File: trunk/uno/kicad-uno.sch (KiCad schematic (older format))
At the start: 16 parts, among them J1 RESET_EN, SW1 RESET

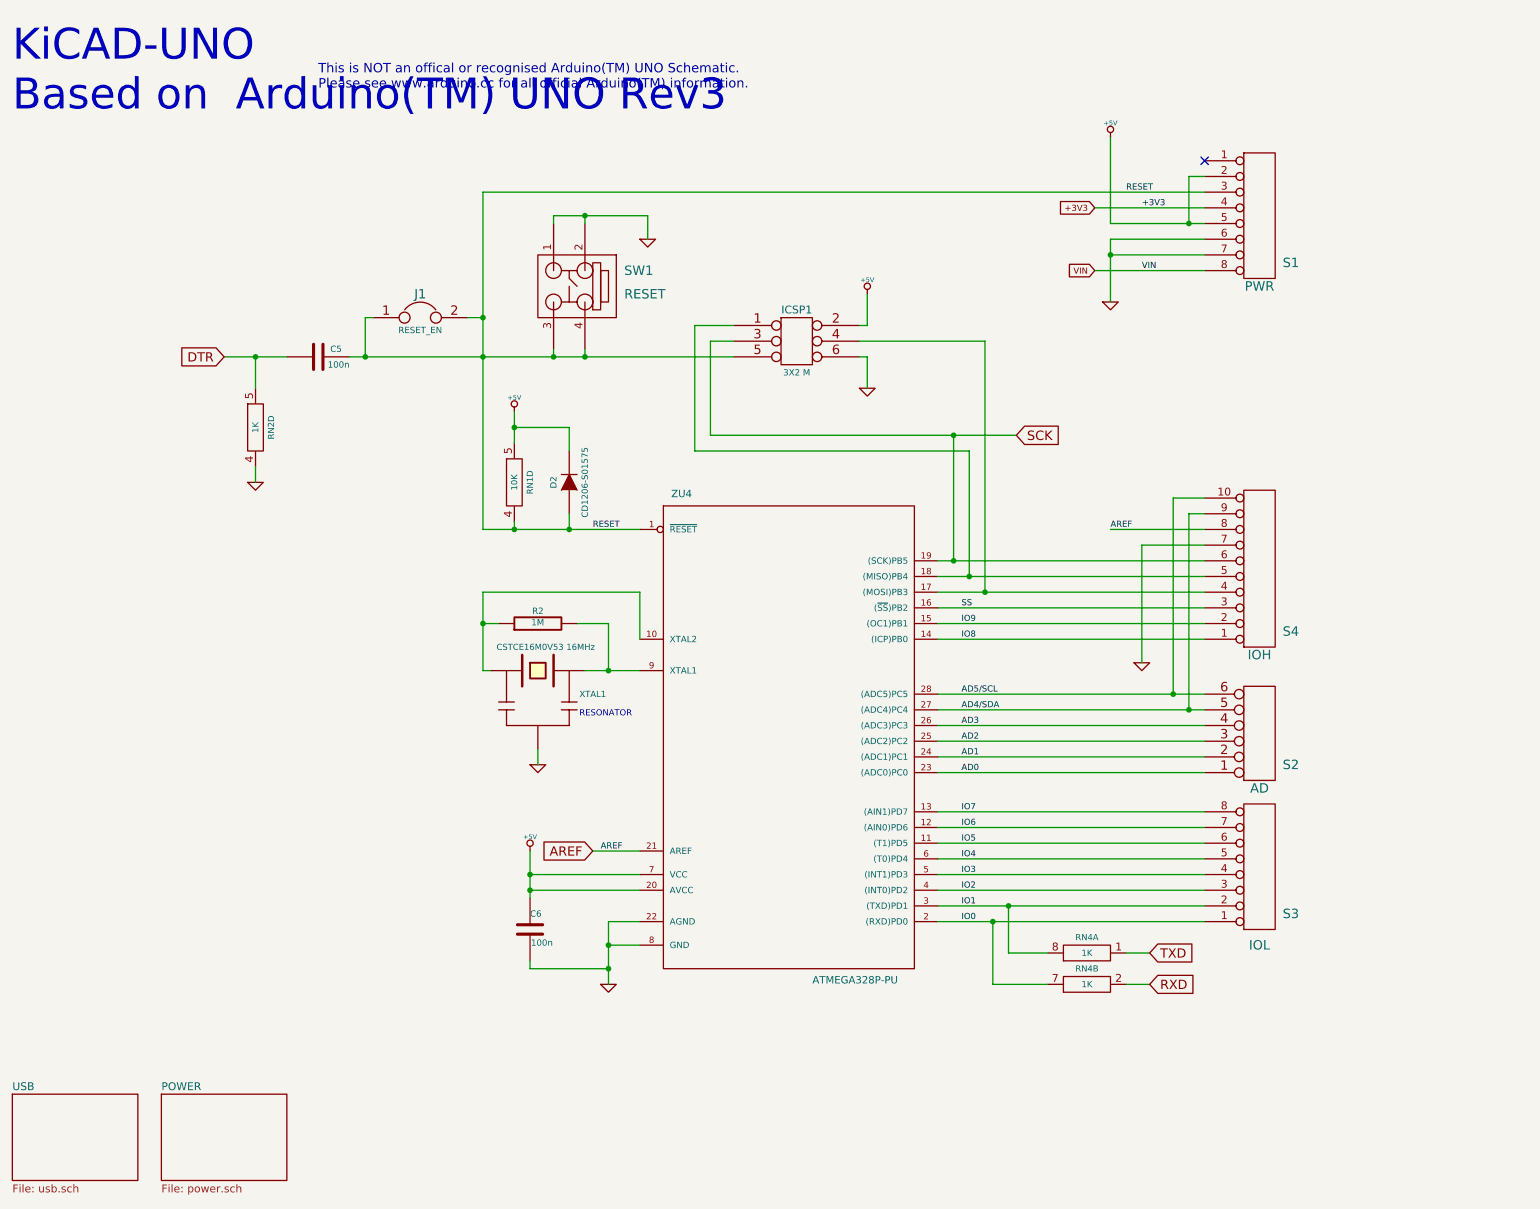
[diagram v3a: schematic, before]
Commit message: About half the comoponents placed, in the exact same location as the UNO Rev3 reference design, except I changed the USB socket to a mini.
A number of minor schematic errors were corrected, around the pin 
numbering of the four resistor network chips.
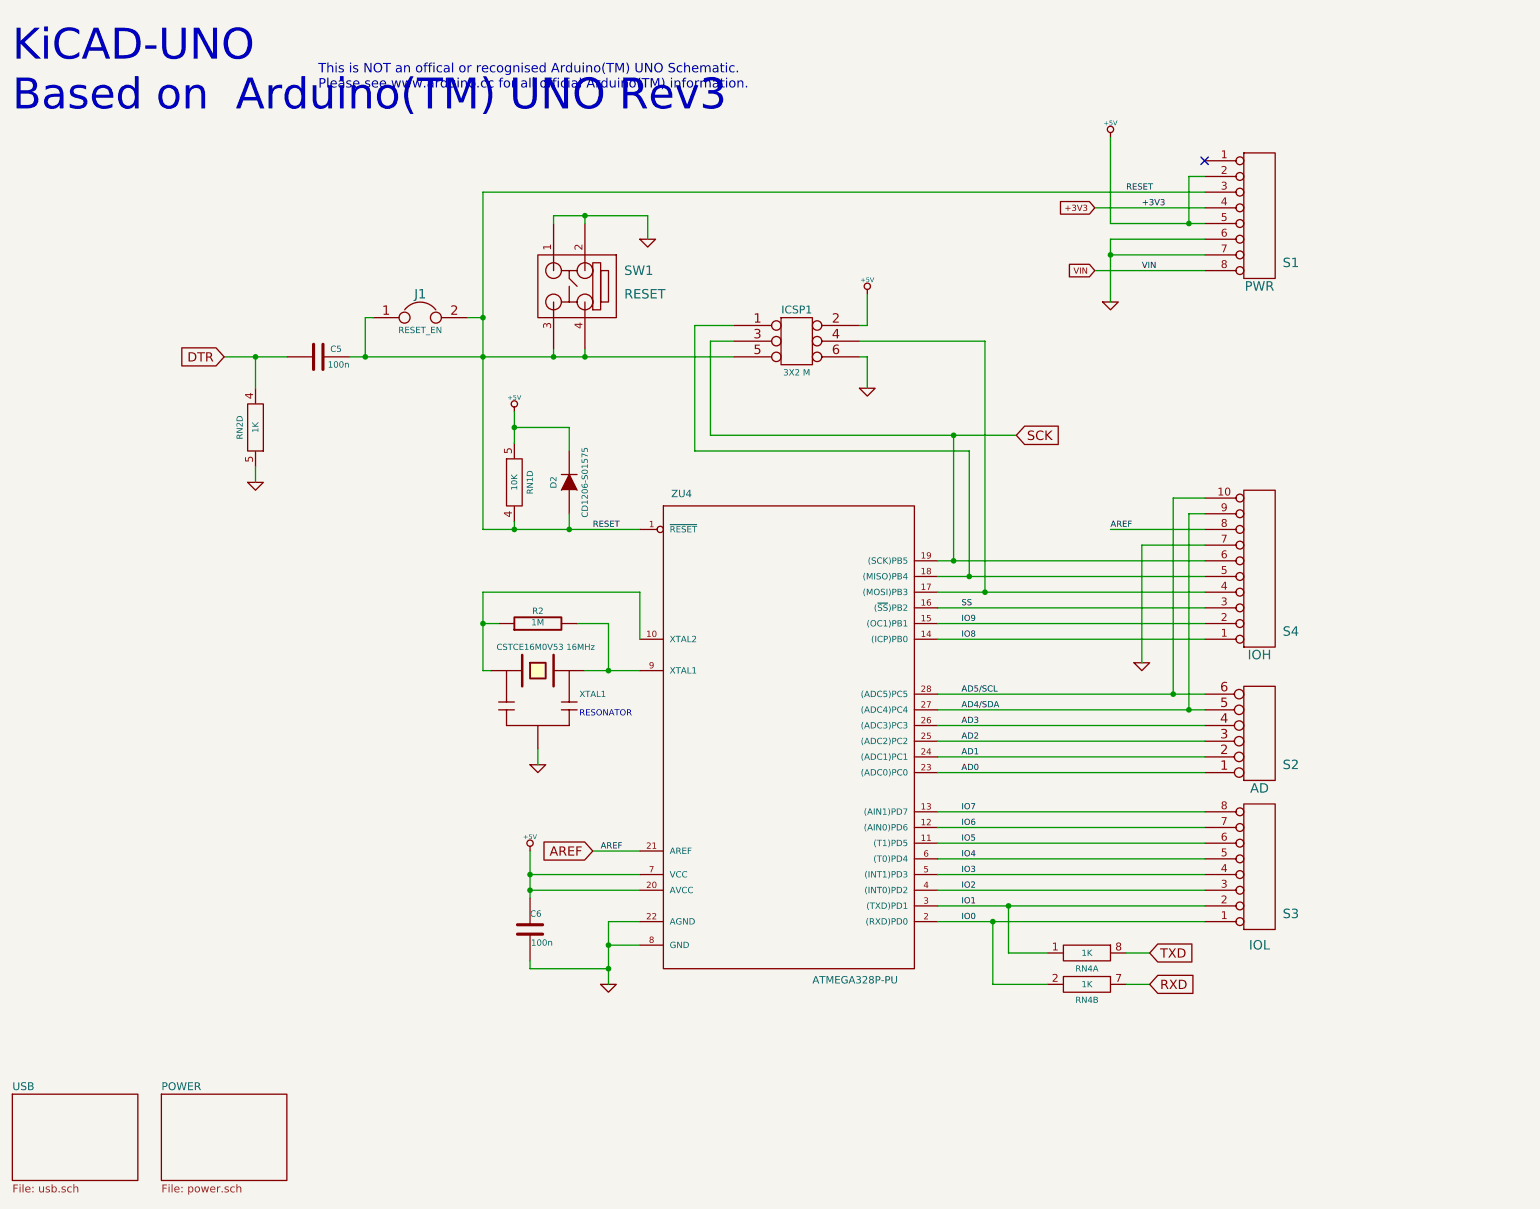
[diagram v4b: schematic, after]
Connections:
- net DTR: now also RN2.4 (3); no longer RN2.5 (6)
- net GND: now also RN2.5 (6); no longer RN2.4 (3)
- net IO0: now also RN4.2 (3); no longer RN4.7 (6)
- net IO1: now also RN4.1 (3); no longer RN4.8 (6)
- net RXD: now also RN4.7 (6); no longer RN4.2 (3)
- net TXD: now also RN4.8 (6); no longer RN4.1 (3)
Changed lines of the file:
@@
 F 3 "" H 2300 2850 60  0000 C CNN
 	4    2300 2850
-	1    0    0    -1
+	-1   0    0    1
 $EndComp
 $Comp
@@
 F 3 "" H 7600 6200 60  0000 C CNN
 	1    7600 6200
-	0    -1   -1   0
+	0    1    1    0
 $EndComp
 $Comp
@@
 F 3 "" H 7600 6400 60  0000 C CNN
 	2    7600 6400
-	0    -1   -1   0
+	0    1    1    0
 $EndComp
 $EndSCHEMATC

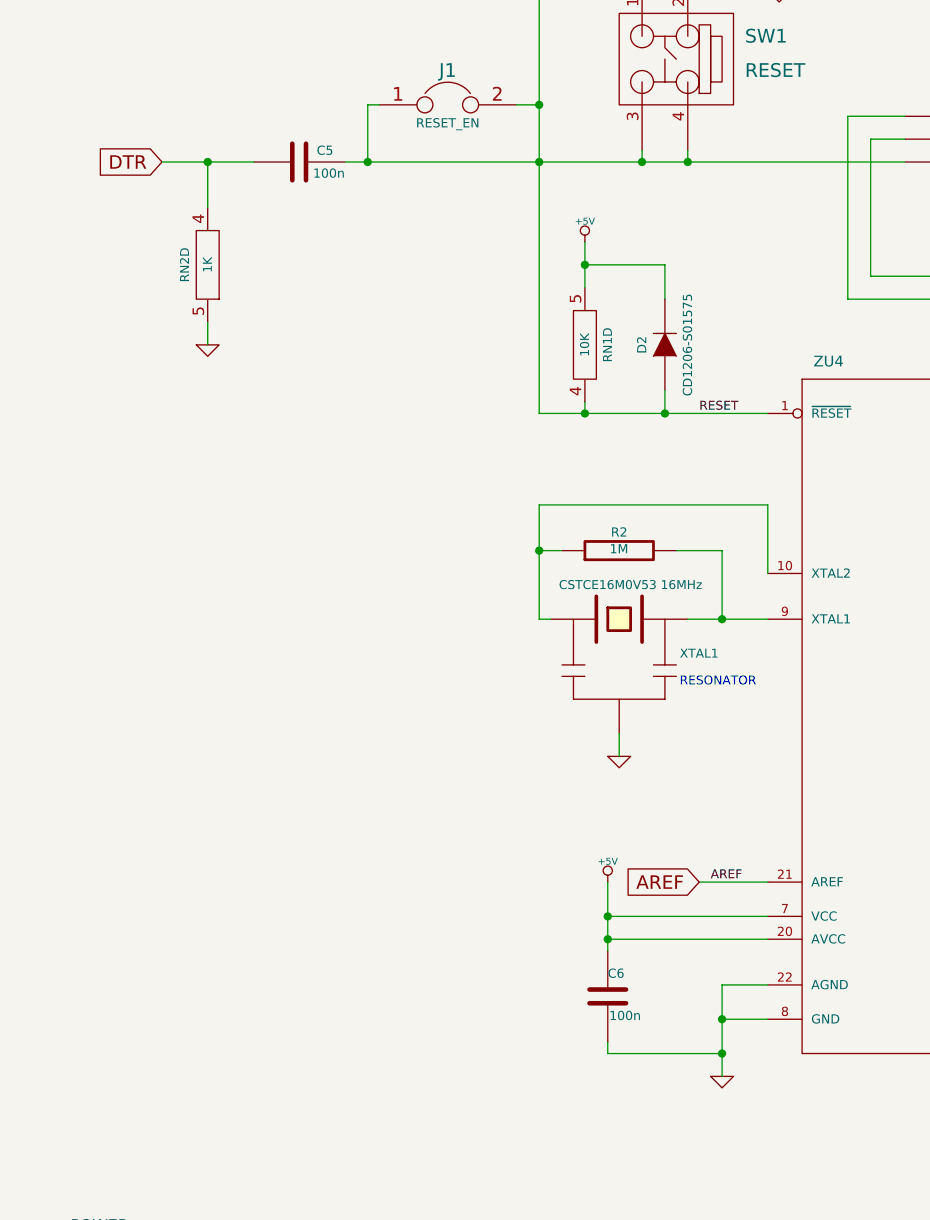
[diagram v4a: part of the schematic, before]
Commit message: All components placed. Some routing started.
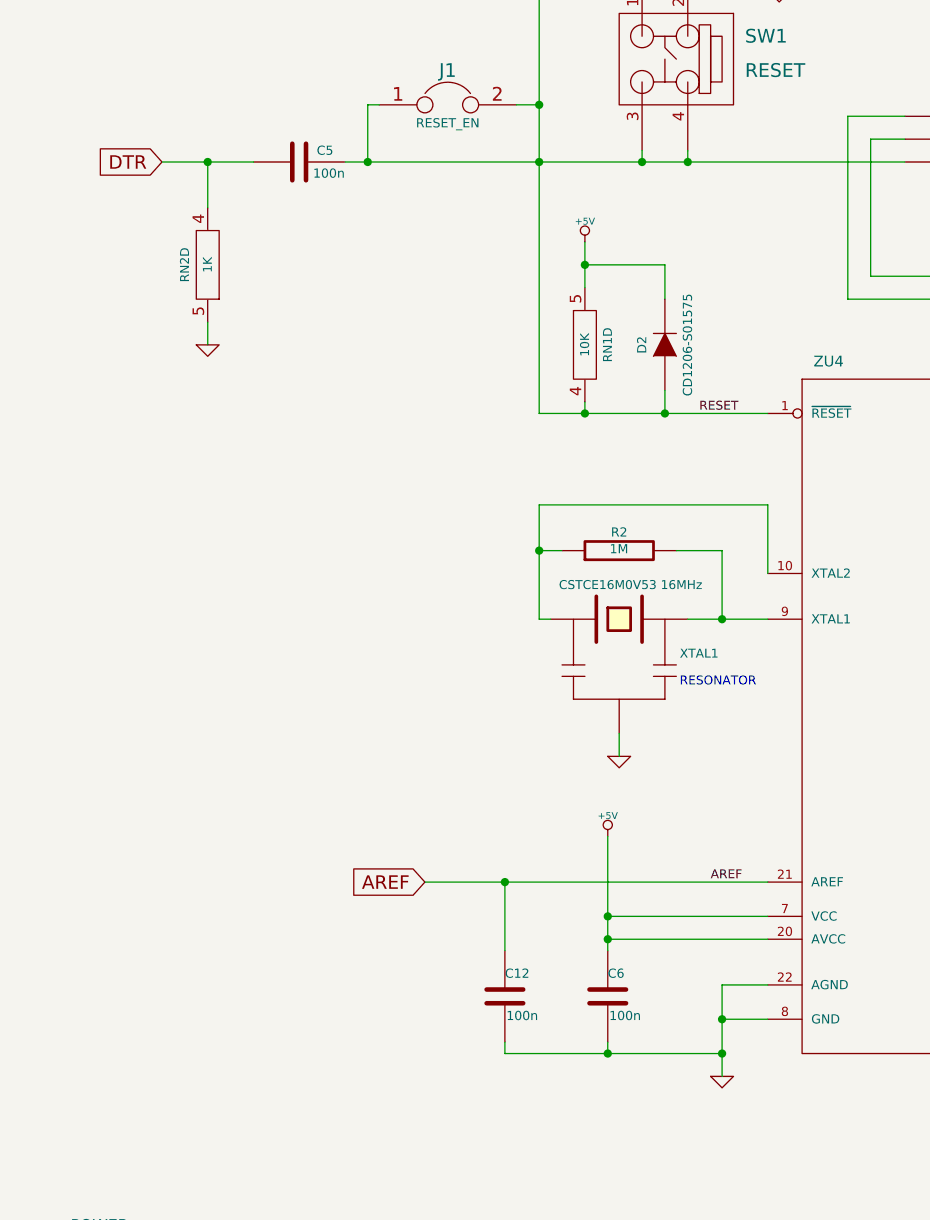
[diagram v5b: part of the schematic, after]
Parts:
- added C12: 100n, SM0603_Capa, symbol C
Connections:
- net AREF: now also C12.1
- net GND: now also C12.2
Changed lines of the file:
@@
 Sheet 1 3
 Title "KiCADuino UNO Rev3"
-Date "25 jul 2013"
+Date "26 jul 2013"
 Rev "0.1"
 Comp "Gruvin & Co"
@@
 L +5V #PWR01
 U 1 1 51EFB351
-P 4050 5550
-F 0 "#PWR01" H 4050 5640 20  0001 C CNN
-F 1 "+5V" H 4050 5640 30  0000 C CNN
-F 2 "" H 4050 5550 60  0000 C CNN
-F 3 "" H 4050 5550 60  0000 C CNN
-	1    4050 5550
+P 4050 5350
+F 0 "#PWR01" H 4050 5440 20  0001 C CNN
+F 1 "+5V" H 4050 5440 30  0000 C CNN
+F 2 "" H 4050 5350 60  0000 C CNN
+F 3 "" H 4050 5350 60  0000 C CNN
+	1    4050 5350
 	1    0    0    -1
 $EndComp
@@
 Text GLabel 2100 2400 0    59   Input ~ 0
 DTR
-Text GLabel 4450 5550 0    59   Input ~ 0
+Text GLabel 3250 5550 0    59   Input ~ 0
 AREF
 $Comp
@@
 Connection ~ 3750 4100
 Wire Wire Line
-	4750 5550 4450 5550
+	4750 5550 3250 5550
 Wire Wire Line
 	4750 5700 4050 5700
 Wire Wire Line
-	4050 5550 4050 5850
+	4050 5350 4050 5850
 Wire Wire Line
 	4050 5800 4750 5800
@@
 	4050 6250 4050 6300
 Wire Wire Line
-	4050 6300 4550 6300
+	3600 6300 4550 6300
 Connection ~ 4550 6300
 Wire Wire Line
@@
 Connection ~ 3000 2400
 Wire Wire Line
-	2500 2400 2100 2400
+	2100 2400 2500 2400
 Wire Wire Line
 	8350 1250 8250 1250
@@
 	0    1    1    0
 $EndComp
+$Comp
+L C C12
+U 1 1 51F20CB4
+P 3600 6050
+F 0 "C12" H 3600 6150 40  0000 L CNN
+F 1 "100n" H 3606 5965 40  0000 L CNN
+F 2 "SM0603_Capa" H 3638 5900 30  0001 C CNN
+F 3 "~" H 3600 6050 60  0000 C CNN
+	1    3600 6050
+	1    0    0    -1
+$EndComp
+Wire Wire Line
+	3600 6250 3600 6300
+Connection ~ 4050 6300
+Wire Wire Line
+	3600 5850 3600 5550
+Connection ~ 3600 5550
 $EndSCHEMATC

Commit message: Board fully completed v1.0.
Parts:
- S1: symbol CONN_8 -> CONN_6
- renumbered XTAL1 to X1, ZU4 to ZU1
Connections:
- net +3V3: now also S1.2; no longer S1.4 (P4)
- net +5V: now also S1.3; no longer S1.2 (P2), S1.5 (P5)
- net GND: now also S1.4, S1.5; no longer S1.6 (P6), S1.7 (P7)
- net RESET: now also S1.1; no longer S1.3 (P3)
- net VIN: now also S1.6; no longer S1.8 (P8)
- no-connect marks 1 -> 0
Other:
- note added: "This socket was an 8-way on the \noriginal Rev3 schematic. But it\nBecame 6-way on all future versions."
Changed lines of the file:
@@
 encoding utf-8
 Sheet 1 3
-Title "KiCADuino UNO Rev3"
-Date "26 jul 2013"
-Rev "0.1"
+Title "KiCADuino (based on UNO Rev3)"
+Date "27 jul 2013"
+Rev "v1.0"
 Comp "Gruvin & Co"
 Comment1 ""
@@
 $EndComp
 $Comp
-L RESONATOR XTAL1
+L RESONATOR X1
 U 1 1 51EFA161
 P 4100 4400
-F 0 "XTAL1" H 4450 4250 39  0000 C CNN
+F 0 "X1" H 4450 4250 39  0000 C CNN
 F 1 "CSTCE16M0V53 16MHz" H 4150 4550 39  0000 C CNN
 F 2 "" H 4100 4400 60  0001 C CNN
@@
 $EndComp
 $Comp
-L ATMEGA328P-PU ZU4
+L ATMEGA328P-PU ZU1
 U 1 1 51EF9E19
 P 5650 4800
-F 0 "ZU4" H 4950 6300 47  0000 L BNN
+F 0 "ZU1" H 4950 6300 47  0000 L BNN
 F 1 "ATMEGA328P-PU" H 5850 3200 47  0000 L BNN
 F 2 "DIP28" H 5650 4850 59  0001 C CNB
@@
 $EndComp
 $Comp
-L CONN_8 S1
+L CONN_6 S1
 U 1 1 51EFBF13
-P 8700 1500
-F 0 "S1" H 8900 1200 60  0000 C CNN
-F 1 "PWR" H 8700 1050 60  0000 C CNN
-F 2 "" H 8700 1500 60  0001 C CNN
-F 3 "" H 8700 1500 60  0000 C CNN
-	1    8700 1500
-	1    0    0    -1
-$EndComp
-NoConn ~ 8350 1150
+P 8700 1600
+F 0 "S1" H 8900 1350 60  0000 C CNN
+F 1 "PWR" H 8700 1200 60  0000 C CNN
+F 2 "" H 8700 1600 60  0001 C CNN
+F 3 "" H 8700 1600 60  0000 C CNN
+	1    8700 1600
+	1    0    0    -1
+$EndComp
 $Comp
 L +5V #PWR08
@@
 	2100 2400 2500 2400
 Wire Wire Line
-	8350 1250 8250 1250
-Wire Wire Line
-	8250 1250 8250 1550
-Wire Wire Line
 	7750 1550 8350 1550
 Wire Wire Line
 	7750 1550 7750 1000
-Connection ~ 8250 1550
 Wire Wire Line
 	8350 1350 3750 1350
@@
 	3600 5850 3600 5550
 Connection ~ 3600 5550
+Text Notes 8900 1500 0    43   ~ 0
+This socket was an 8-way on the \noriginal Rev3 schematic. But it\nBecame 6-way on all future versions.
 $EndSCHEMATC
